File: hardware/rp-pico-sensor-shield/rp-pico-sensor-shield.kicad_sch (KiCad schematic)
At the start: 33 parts, among them J1 Barrel_Jack, J10 Conn_01x04, J11 Conn_01x04, J12 Conn_01x04, J13 Conn_01x04, J14 Conn_01x04, J15 Conn_01x04, J16 Conn_01x04, J17 Conn_01x04, J18 Conn_01x03, J19 Conn_01x03, J2 AGND, J20 Conn_01x03, J21 Conn_01x03, J22 Conn_01x03, J23 Conn_01x03, J24 SM04B-SRSS-TB, J25 Conn_01x04, J26 Conn_01x04, J27 Conn_01x03, J3 Conn_01x04, J4 Conn_01x04, J5 Conn_01x04, J6 Conn_01x04, J7 Conn_01x04, J8 Conn_01x04, J9 Conn_01x04, Q1 DMG2305UX, SW1 SW_Push, U1 Pico, U2 NCP1117-5.0_SOT223

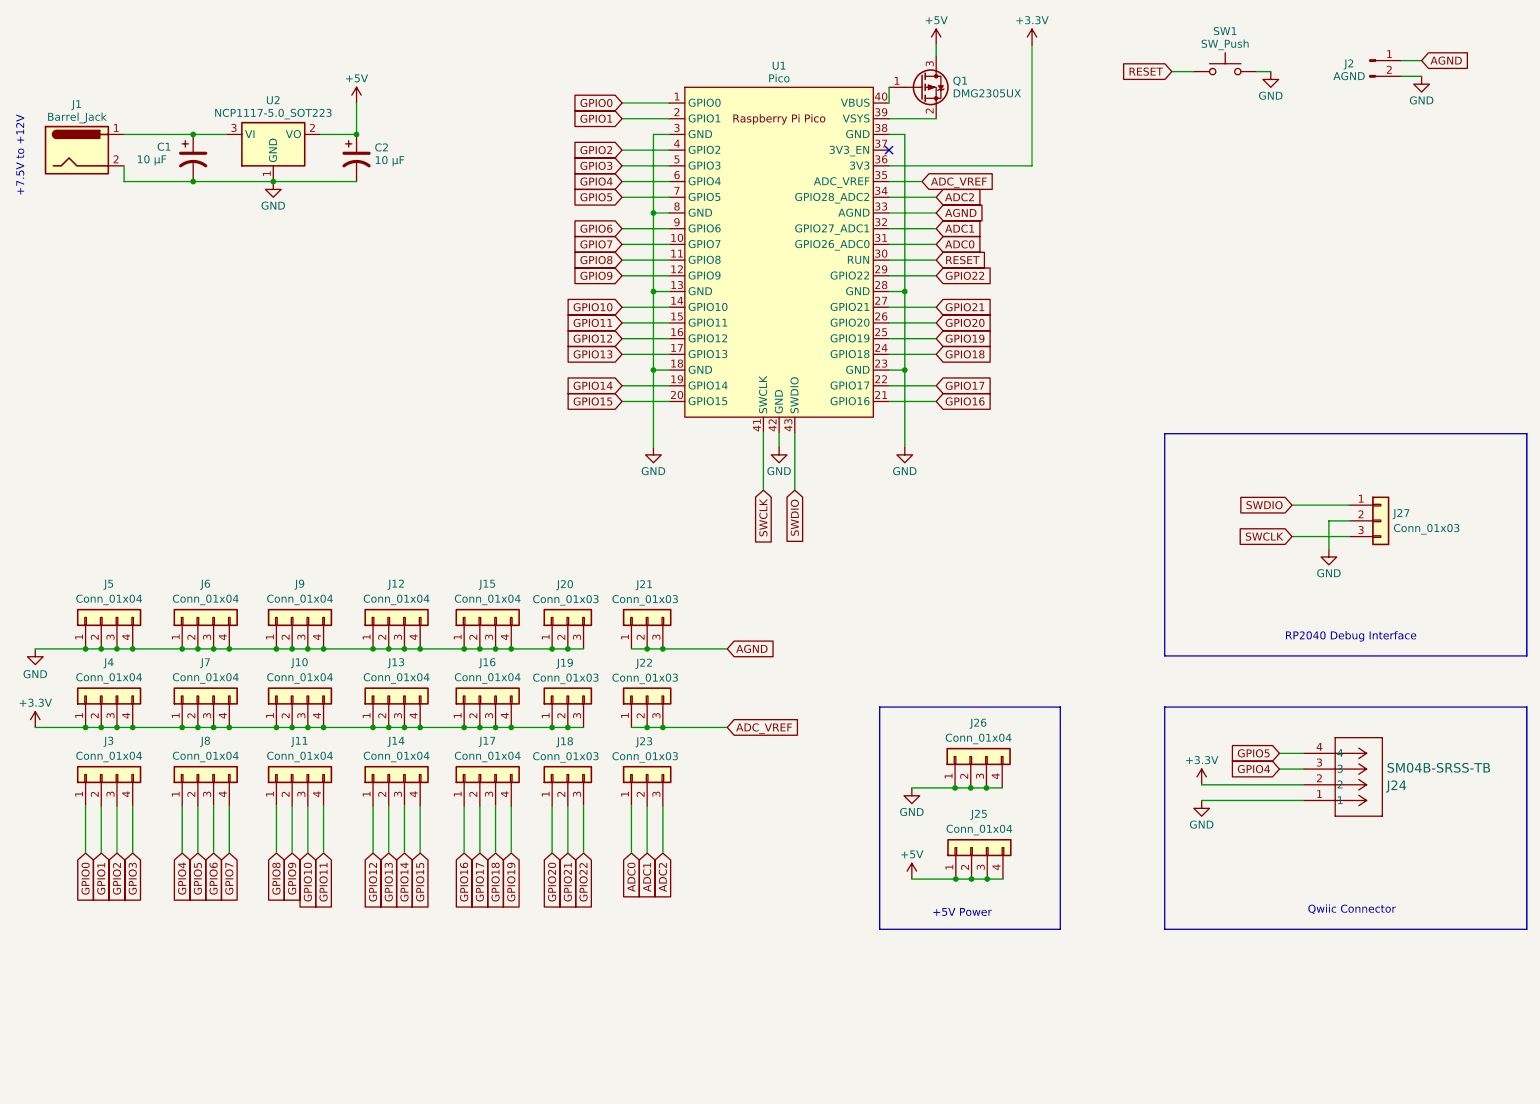
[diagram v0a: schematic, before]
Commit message: added pid controller class
also updated schematic of sensor board to have two IC2 Qwiic connectors
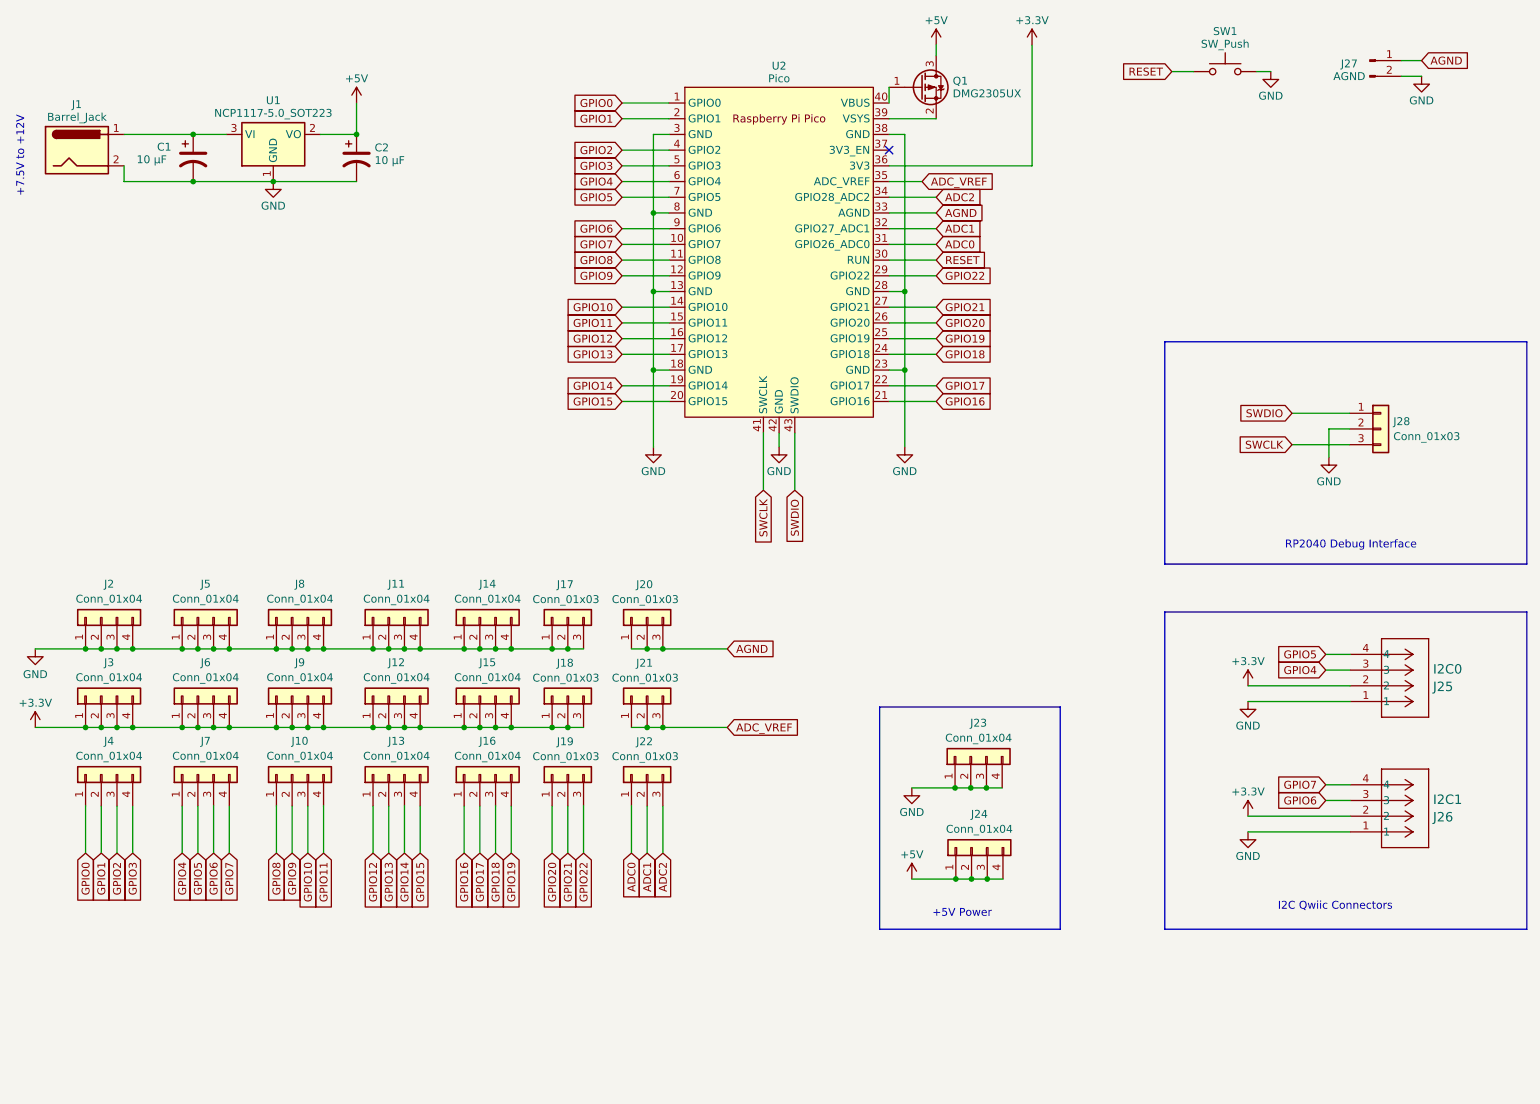
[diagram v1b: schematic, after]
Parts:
- added J25: I2C0, SM04B-SRSS-TB:CONN_SM04B-SRSS-TB_JST, symbol SM04B-SRSS-TB:SM04B-SRSS-TB
- J26: renamed from J24; value SM04B-SRSS-TB -> I2C1
- renumbered J11 to J10, J12 to J11, J13 to J12, J14 to J13, J15 to J14, J16 to J15, J17 to J16, J20 to J17, J19 to J18, J18 to J19, J5 to J2, J21 to J20, J22 to J21, J23 to J22, J26 to J23, J25 to J24, J2 to J27, J27 to J28, J4 to J3, J3 to J4, J6 to J5, J7 to J6, J8 to J7, J9 to J8, J10 to J9, U2 to U1, U1 to U2
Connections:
- net +3.3V: now also J25.2
- net GND: now also J25.1
- net GPIO4: now also J25.3; no longer J26.3
- net GPIO5: now also J25.4; no longer J26.4
- net GPIO6: now also J26.3
- net GPIO7: now also J26.4
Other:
- note added: "I2C Qwiic Connectors"
- note removed: "Qwiic Connector"
- moved on the sheet: J26, J28

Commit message: finalized pin wiring
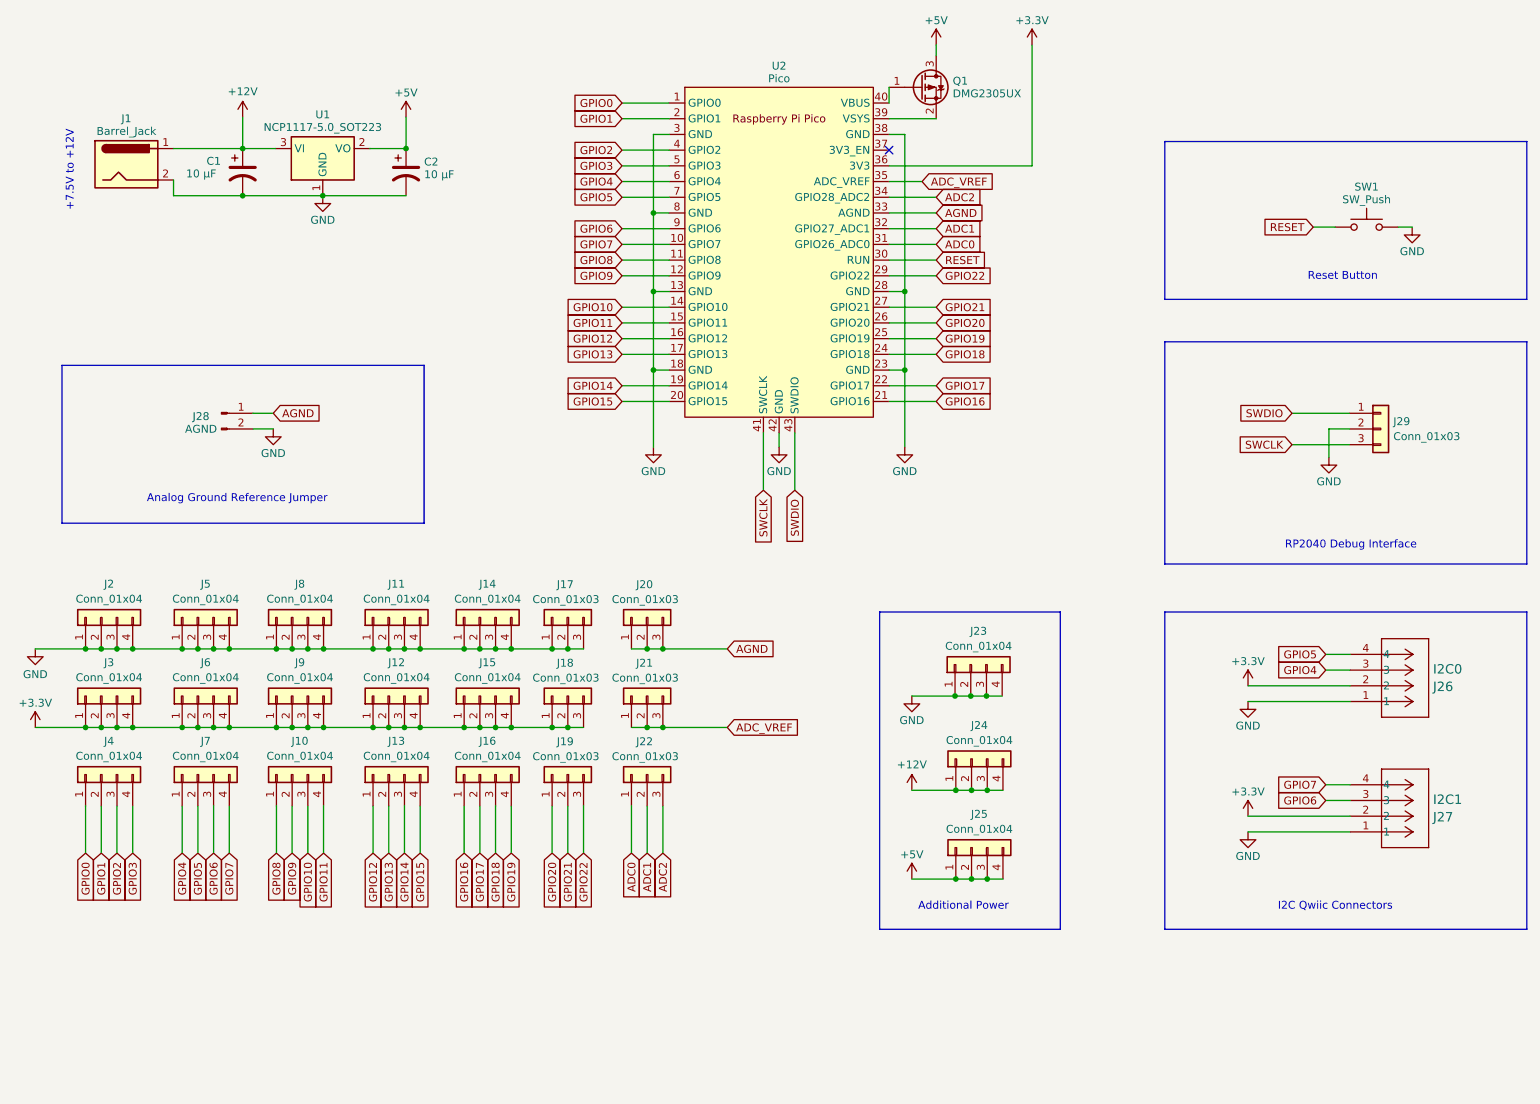
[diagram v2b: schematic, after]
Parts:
- added J24: Conn_01x04, Connector_PinHeader_2.54mm:PinHeader_1x04_P2.54mm_Vertical, symbol Connector_Generic:Conn_01x04
- C1, C2: footprint Capacitor_SMD:C_0603_1608Metric -> Capacitor_SMD:C_1206_3216Metric_Pad1.33x1.80mm_HandSolder
- J29: renamed from J28; footprint Connector_PinHeader_2.54mm:PinHeader_1x03_P2.54mm_Horizontal -> Connector_JST:JST_SH_BM03B-SRSS-TB_1x03-1MP_P1.00mm_Vertical
- renumbered J24 to J25, J25 to J26, J26 to J27, J27 to J28
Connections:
- net +12V: now reaches C1.1, J1.1, U1.3 (VI)
- net +12V: now also J24.1 (Pin_1), J24.2 (Pin_2), J24.3 (Pin_3), J24.4 (Pin_4)
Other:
- note added: "Additional Power"
- note added: "Analog Ground Reference Jumper"
- note added: "Reset Button"
- note removed: "+5V Power"
- moved on the sheet: C1, C2, J1, J23, J28, SW1, U1

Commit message: wip update to rp2040 sensor shield
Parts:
- removed J24: Conn_01x04, Connector_PinHeader_2.54mm:PinHeader_1x04_P2.54mm_Vertical, symbol Connector_Generic:Conn_01x04
- added J24: Screw Terminal, CONN2_1760510000_WED:CONN2_1760510000_WED, symbol CONN2_1760510000_WED:1760510000
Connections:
- net +12V: now also J24.1
- net GND: now also J24.2
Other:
- moved on the sheet: J23

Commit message: updated sensor shield layout
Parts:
- added R1, R2: 100, Resistor_SMD:R_1206_3216Metric_Pad1.30x1.75mm_HandSolder, symbol Device:R
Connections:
- net SWCLK: now also R2.1; no longer J29.3 (Pin_3)
- net SWDIO: now also R1.1; no longer J29.1 (Pin_1)
- new net: J29.1 (Pin_1), R2.2
- new net: J29.3 (Pin_3), R1.2
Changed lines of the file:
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@@
     )
   )
-  (global_label "SWDIO" (shape input) (at 226.949 78.359 180) (fields_autoplaced)
-    (effects (font (size 1.27 1.27)) (justify right))
-    (property "Intersheetrefs" "${INTERSHEET_REFS}" (at 218.0976 78.359 0)
+  (global_label "SWDIO" (shape input) (at 219.329 83.439 180) (fields_autoplaced)
+    (effects (font (size 1.27 1.27)) (justify right))
+    (property "Intersheetrefs" "${INTERSHEET_REFS}" (at 210.4776 83.439 0)
       (effects (font (size 1.27 1.27)) (justify right) hide)
     )
@@
     )
   )
-  (global_label "SWCLK" (shape input) (at 226.949 83.439 180) (fields_autoplaced)
-    (effects (font (size 1.27 1.27)) (justify right))
-    (property "Intersheetrefs" "${INTERSHEET_REFS}" (at 217.7348 83.439 0)
+  (global_label "SWCLK" (shape input) (at 219.329 78.359 180) (fields_autoplaced)
+    (effects (font (size 1.27 1.27)) (justify right))
+    (property "Intersheetrefs" "${INTERSHEET_REFS}" (at 210.1148 78.359 0)
       (effects (font (size 1.27 1.27)) (justify right) hide)
     )
@@
     )
   )
+  (symbol (lib_id "Device:R") (at 223.139 78.359 90) (unit 1)
+    (in_bom yes) (on_board yes) (dnp no)
+    (property "Reference" "R2" (at 223.1644 76.3016 90)
+      (effects (font (size 1.27 1.27)))
+    )
+    (property "Value" "100" (at 223.1644 78.3844 90)
+      (effects (font (size 1.27 1.27)))
+    )
+    (property "Footprint" "Resistor_SMD:R_1206_3216Metric_Pad1.30x1.75mm_HandSolder" (at 223.139 80.137 90)
+      (effects (font (size 1.27 1.27)) hide)
+    )
+    (property "Datasheet" "~" (at 223.139 78.359 0)
+      (effects (font (size 1.27 1.27)) hide)
+    )
+    (pin "1")
+    (pin "2")
+    (instances
+      (project "rp-pico-sensor-shield"
+        (path "/01191561-9ded-4746-bfa0-1bc8653df791"
+          (reference "R2") (unit 1)
+        )
+      )
+    )
+  )
   (symbol (lib_id "Connector_Generic:Conn_01x04") (at 65.278 111.379 90) (unit 1)
     (in_bom yes) (on_board yes) (dnp no) (fields_autoplaced)
@@
         )
       )
+    )
+  )
+  (symbol (lib_id "Device:R") (at 223.139 83.439 90) (unit 1)
+    (in_bom yes) (on_board yes) (dnp no)
+    (property "Reference" "R1" (at 223.1644 85.8012 90)
+      (effects (font (size 1.27 1.27)))
+    )
+    (property "Value" "100" (at 223.1644 83.5152 90)
+      (effects (font (size 1.27 1.27)))
+    )
+    (property "Footprint" "Resistor_SMD:R_1206_3216Metric_Pad1.30x1.75mm_HandSolder" (at 223.139 85.217 90)
+      (effects (font (size 1.27 1.27)) hide)
+    )
+    (property "Datasheet" "~" (at 223.139 83.439 0)
+      (effects (font (size 1.27 1.27)) hide)
+    )
+    (pin "1")
+    (pin "2")
+    (instances
+      (project "rp-pico-sensor-shield"
+        (path "/01191561-9ded-4746-bfa0-1bc8653df791"
+          (reference "R1") (unit 1)
+        )
+      )

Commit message: kicad v8 upgrade
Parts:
- added H1, H2, H3, H4: MountingHole, MountingHole:MountingHole_3.2mm_M3_ISO7380_Pad, symbol Mechanical:MountingHole
- added J30: Conn_01x03, Connector_PinHeader_1.00mm:PinHeader_1x03_P1.00mm_Vertical, symbol Connector_Generic:Conn_01x03
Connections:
- net GND: now also J30.2 (Pin_2)
- net SWCLK: now also J30.1 (Pin_1)
- net SWDIO: now also J30.3 (Pin_3)
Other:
- note added: "Raspberry Pi Pico W SWD Connector"
